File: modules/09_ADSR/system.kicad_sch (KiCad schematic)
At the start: 1 part

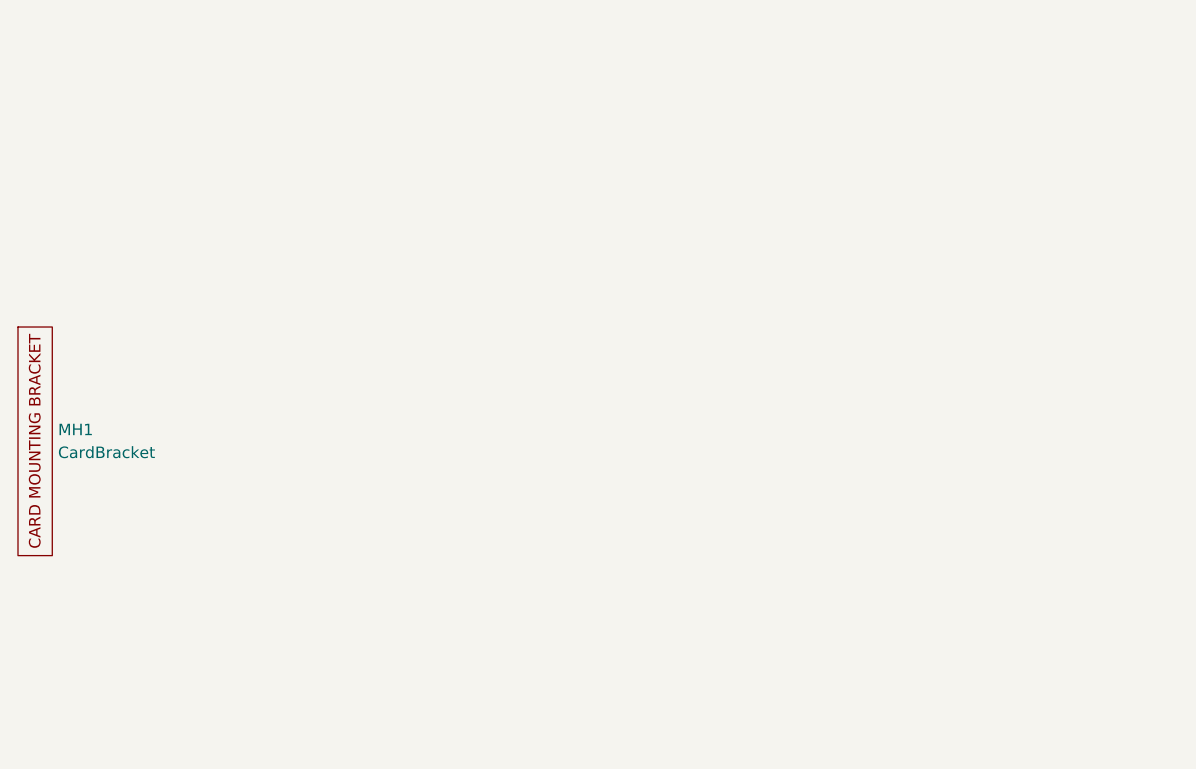
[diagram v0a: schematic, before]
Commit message: adsr routing
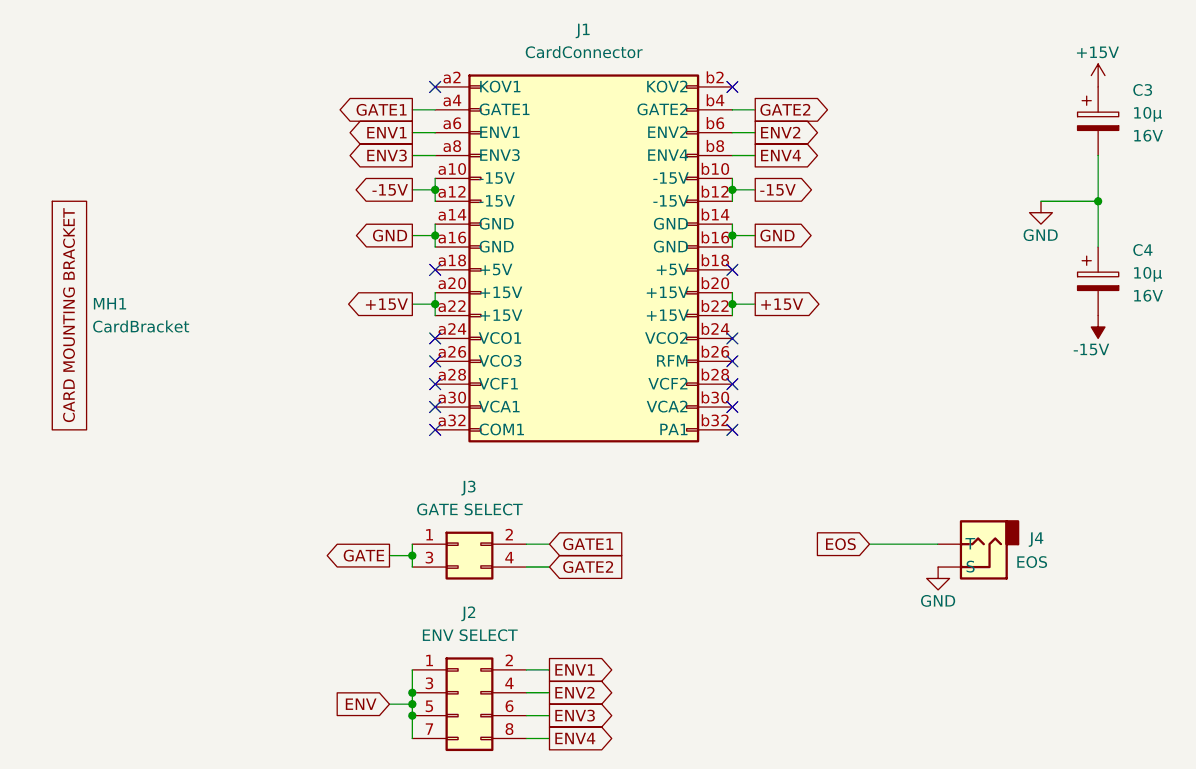
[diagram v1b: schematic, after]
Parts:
- removed MH1: CardBracket, FormantKO:Card_Bracket, symbol FormantKO:Card_Bracket
- added C3, C4: 10µ, FormantKO:CP_Axial_600, symbol FormantKO:C_Polarized
- added J1: CardConnector, FormantKO:Card_Connector, symbol FormantKO:CardConnector
- added J2: ENV SELECT, Connector_PinHeader_2.54mm:PinHeader_2x04_P2.54mm_Vertical, symbol Connector_Generic:Conn_02x04_Odd_Even
- added J3: GATE SELECT, Connector_PinHeader_2.54mm:PinHeader_2x02_P2.54mm_Vertical, symbol Connector_Generic:Conn_02x02_Odd_Even
- added J4: EOS, FormantKO:Panel_Connector_1x02, symbol FormantKO:MonoJack
- added MH1: CardBracket, FormantKO:Card_Bracket, symbol FormantKO:CardBracket
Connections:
- new net +15V: C3.1, J1.a20 (+15V), J1.a22 (+15V), J1.b20 (+15V), J1.b22 (+15V)
- new net -15V: C4.2, J1.a10 (-15V), J1.a12 (-15V), J1.b10 (-15V), J1.b12 (-15V)
- new net ENV: J2.1 (Pin_1), J2.3 (Pin_3), J2.5 (Pin_5), J2.7 (Pin_7)
- new net ENV1: J1.a6 (ENV1), J2.2 (Pin_2)
- new net ENV2: J1.b6 (ENV2), J2.4 (Pin_4)
- new net ENV3: J1.a8 (ENV3), J2.6 (Pin_6)
- new net ENV4: J1.b8 (ENV4), J2.8 (Pin_8)
- new net EOS: J4.2 (T)
- new net GATE: J3.1 (Pin_1), J3.3 (Pin_3)
- new net GATE1: J1.a4 (GATE1), J3.2 (Pin_2)
- new net GATE2: J1.b4 (GATE2), J3.4 (Pin_4)
- new net GND: C3.2, C4.1, J1.a14 (GND), J1.a16 (GND), J1.b14 (GND), J1.b16 (GND), J4.1 (S)
- no-connect marks 0 -> 14
